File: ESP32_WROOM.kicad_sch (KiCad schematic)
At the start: 11 parts, among them J7 Programming Socket, Q1 NPN, Q2 NPN, SW1 EN, SW2 EN, U11 NTS0104GU12_115, U6 ESP32-WROOM-32E

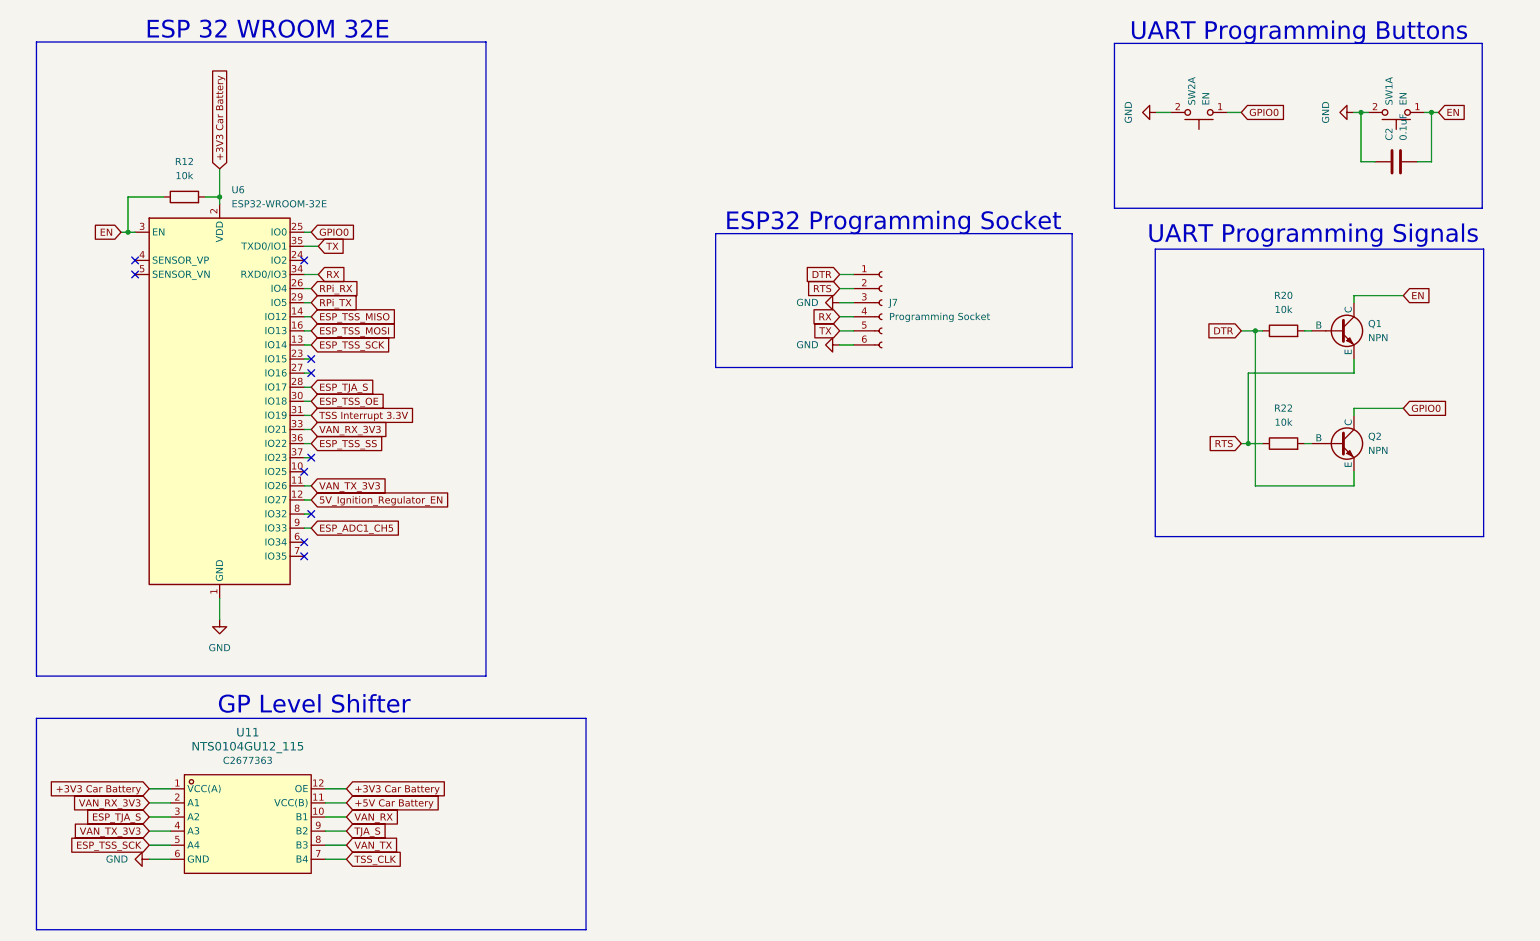
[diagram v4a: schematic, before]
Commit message: changed power regulators, updated PCB
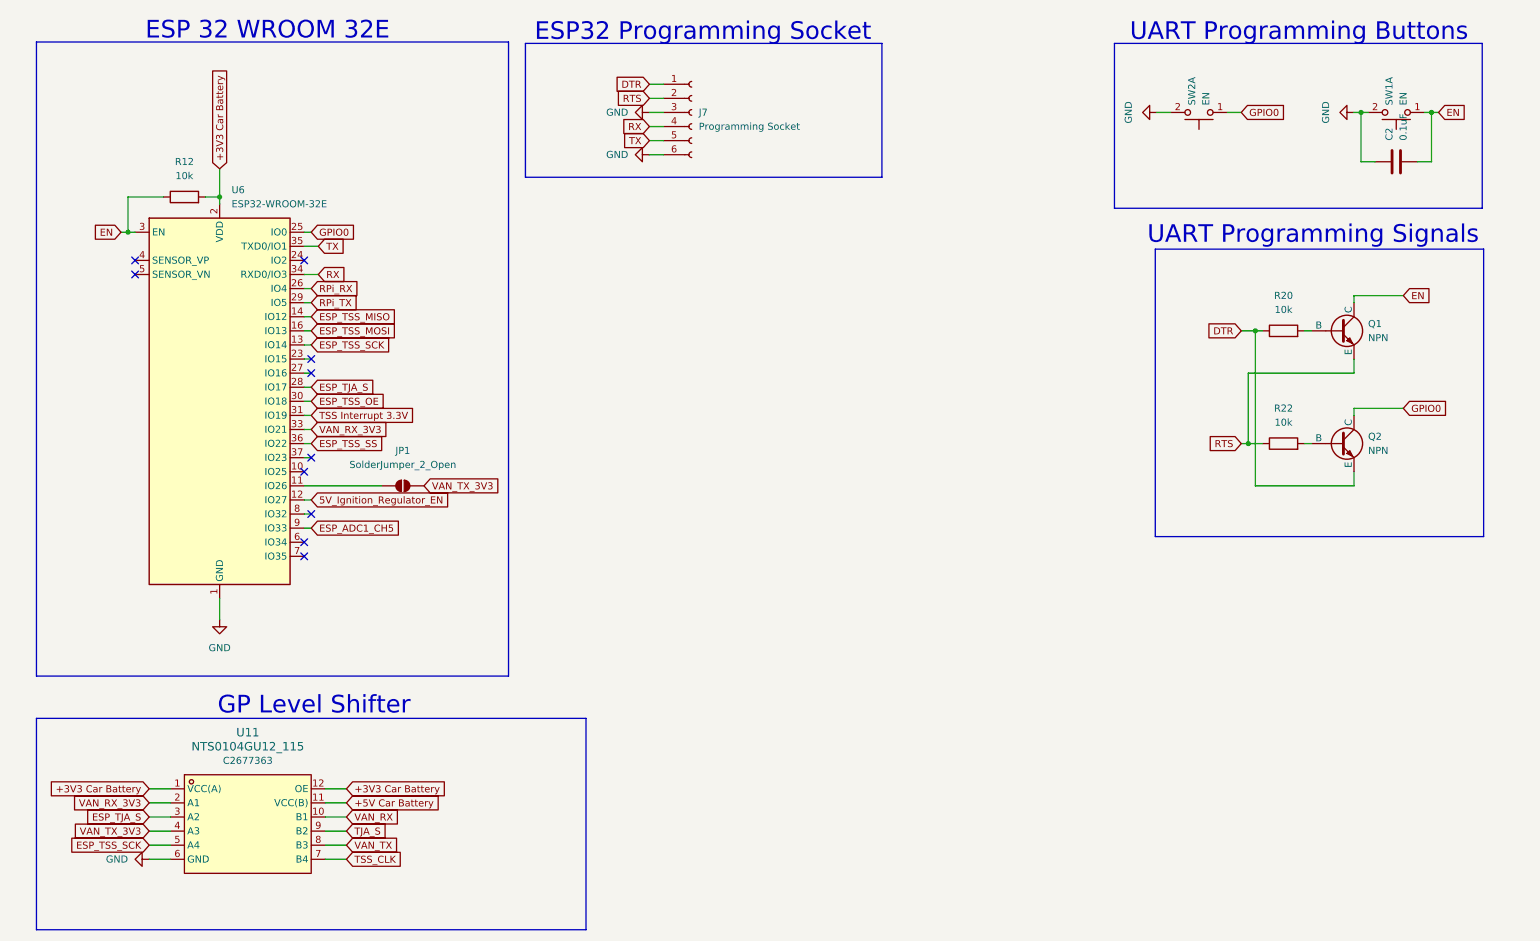
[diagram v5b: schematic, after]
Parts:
- added JP1: SolderJumper_2_Open, Jumper:SolderJumper-2_P1.3mm_Open_Pad1.0x1.5mm, symbol Jumper:SolderJumper_2_Open
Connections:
- net VAN_TX_3V3: now also JP1.2 (B); no longer U6.11 (IO26)
- new net: JP1.1 (A), U6.11 (IO26)
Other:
- moved on the sheet: J7
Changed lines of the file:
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@@
 	)
 	(rectangle
-		(start 140.208 52.324)
-		(end 204.47 76.454)
+		(start 105.918 18.034)
+		(end 170.18 42.164)
 		(stroke
 			(width 0)
@@
 	(rectangle
 		(start 17.78 17.78)
-		(end 98.806 132.08)
+		(end 102.87 132.08)
 		(stroke
 			(width 0)
@@
 	(text "ESP32 Programming Socket\n"
 		(exclude_from_sim no)
-		(at 172.212 50.292 0)
+		(at 137.922 16.002 0)
 		(effects
 			(font
@@
 	(wire
 		(pts
-			(xy 162.56 64.77) (xy 165.1 64.77)
+			(xy 128.27 30.48) (xy 130.81 30.48)
 		)
 		(stroke
@@
 	(wire
 		(pts
-			(xy 66.04 97.79) (xy 67.31 97.79)
+			(xy 66.04 97.79) (xy 80.01 97.79)
 		)
 		(stroke
@@
 	(wire
 		(pts
-			(xy 162.56 69.85) (xy 165.1 69.85)
+			(xy 128.27 35.56) (xy 130.81 35.56)
 		)
 		(stroke
@@
 	(wire
 		(pts
-			(xy 162.56 59.69) (xy 165.1 59.69)
+			(xy 128.27 25.4) (xy 130.81 25.4)
 		)
 		(stroke
@@
 	(wire
 		(pts
-			(xy 162.56 67.31) (xy 165.1 67.31)
-		)
-		(stroke
-			(width 0)
-			(type default)
-		)
-	)
-	(wire
-		(pts
-			(xy 162.56 72.39) (xy 165.1 72.39)
+			(xy 128.27 33.02) (xy 130.81 33.02)
+		)
+		(stroke
+			(width 0)
+			(type default)
+		)
+	)
+	(wire
+		(pts
+			(xy 128.27 38.1) (xy 130.81 38.1)
 		)
 		(stroke
@@
 	(wire
 		(pts
-			(xy 162.56 62.23) (xy 165.1 62.23)
+			(xy 128.27 27.94) (xy 130.81 27.94)
 		)
 		(stroke
@@
 	(global_label "TX"
 		(shape input)
-		(at 162.56 69.85 180)
+		(at 128.27 35.56 180)
 		(fields_autoplaced yes)
 		(effects
@@
 		)
 		(property "Intersheetrefs" "${INTERSHEET_REFS}"
-			(at 157.3977 69.85 0)
+			(at 123.1077 35.56 0)
 			(effects
 				(font
@@
 		)
 	)
+	(global_label "VAN_TX_3V3"
+		(shape input)
+		(at 87.63 97.79 0)
+		(fields_autoplaced yes)
+		(effects
+			(font
+				(size 1.27 1.27)
+			)
+			(justify left)
+		)
+		(property "Intersheetrefs" "${INTERSHEET_REFS}"
+			(at 101.7428 97.79 0)
+			(effects
+				(font
+					(size 1.27 1.27)
+				)
+				(justify left)
+				(hide yes)
+			)
+		)
+	)
 	(global_label "EN"
 		(shape input)
@@
 		)
 	)
-	(global_label "VAN_TX_3V3"
-		(shape input)
-		(at 67.31 97.79 0)
-		(fields_autoplaced yes)
-		(effects
-			(font
-				(size 1.27 1.27)
-			)
-			(justify left)
-		)
-		(property "Intersheetrefs" "${INTERSHEET_REFS}"
-			(at 81.4228 97.79 0)
-			(effects
-				(font
-					(size 1.27 1.27)
-				)
-				(justify left)
-				(hide yes)
-			)
-		)
-	)
 	(global_label "EN"
 		(shape input)
@@
 	(global_label "RX"
 		(shape input)
-		(at 162.56 67.31 180)
+		(at 128.27 33.02 180)
 		(fields_autoplaced yes)
 		(effects
@@
 		)
 		(property "Intersheetrefs" "${INTERSHEET_REFS}"
-			(at 157.0953 67.31 0)
+			(at 122.8053 33.02 0)
 			(effects
 				(font
@@
 	(global_label "RTS"
 		(shape input)
-		(at 162.56 62.23 180)
+		(at 128.27 27.94 180)
 		(fields_autoplaced yes)
 		(effects
@@
 		)
 		(property "Intersheetrefs" "${INTERSHEET_REFS}"
-			(at 156.1277 62.23 0)
+			(at 121.8377 27.94 0)
 			(effects
 				(font
@@
 	(global_label "DTR"
 		(shape input)
-		(at 162.56 59.69 180)
+		(at 128.27 25.4 180)
 		(fields_autoplaced yes)
 		(effects
@@
 		)
 		(property "Intersheetrefs" "${INTERSHEET_REFS}"
-			(at 156.0672 59.69 0)
+			(at 121.7772 25.4 0)
 			(effects
 				(font
@@
 	(symbol
 		(lib_id "power:GND")
-		(at 162.56 72.39 270)
+		(at 128.27 38.1 270)
 		(unit 1)
 		(exclude_from_sim no)
@@
 		(fields_autoplaced yes)
 		(property "Reference" "#PWR090"
-			(at 156.21 72.39 0)
+			(at 121.92 38.1 0)
 			(effects
 				(font
@@
 		)
 		(property "Value" "GND"
-			(at 158.75 72.3899 90)
+			(at 124.46 38.0999 90)
 			(effects
 				(font
@@
 		)
 		(property "Footprint" ""
-			(at 162.56 72.39 0)
+			(at 128.27 38.1 0)
 			(effects
 				(font
@@
 		)
 		(property "Datasheet" ""
-			(at 162.56 72.39 0)
+			(at 128.27 38.1 0)
 			(effects
 				(font
@@
 		)
 		(property "Description" "Power symbol creates a global label with name \"GND\" , ground"
-			(at 162.56 72.39 0)
+			(at 128.27 38.1 0)
 			(effects
 				(font
@@
 	)
 	(symbol
+		(lib_id "Jumper:SolderJumper_2_Open")
+		(at 83.82 97.79 0)
+		(unit 1)
+		(exclude_from_sim no)
+		(in_bom no)
+		(on_board yes)
+		(dnp no)
+		(fields_autoplaced yes)
+		(property "Reference" "JP1"
+			(at 83.82 91.44 0)
+			(effects
+				(font
+					(size 1.27 1.27)
+				)
+			)
+		)
+		(property "Value" "SolderJumper_2_Open"
+			(at 83.82 93.98 0)
+			(effects
+				(font
+					(size 1.27 1.27)
+				)
+			)
+		)
+		(property "Footprint" "Jumper:SolderJumper-2_P1.3mm_Open_Pad1.0x1.5mm"
+			(at 83.82 97.79 0)
+			(effects
+				(font
+					(size 1.27 1.27)
+				)
+				(hide yes)
+			)
+		)
+		(property "Datasheet" "~"
+			(at 83.82 97.79 0)
+			(effects
+				(font
+					(size 1.27 1.27)
+				)
+				(hide yes)
+			)
+		)
+		(property "Description" "Solder Jumper, 2-pole, open"
+			(at 83.82 97.79 0)
+			(effects
+				(font
+					(size 1.27 1.27)
+				)
+				(hide yes)
+			)
+		)
+		(pin "2"
+		)
+		(pin "1"
+		)
+		(instances
+			(project ""
+				(path "/3ec17d1d-183f-42c7-9d9d-808fb8c0b5df/821b1801-1173-4ad6-9af8-a86cd2d3359b"
+					(reference "JP1")
+					(unit 1)
+				)
+			)
+		)
+	)
+	(symbol
 		(lib_id "power:GND")
-		(at 162.56 64.77 270)
+		(at 128.27 30.48 270)
 		(unit 1)
 		(exclude_from_sim no)
@@
 		(fields_autoplaced yes)
 		(property "Reference" "#PWR089"
-			(at 156.21 64.77 0)
+			(at 121.92 30.48 0)
 			(effects
 				(font
@@
 		)
 		(property "Value" "GND"
-			(at 158.75 64.7699 90)
+			(at 124.46 30.4799 90)
 			(effects
 				(font
@@
 		)
 		(property "Footprint" ""
-			(at 162.56 64.77 0)
+			(at 128.27 30.48 0)
 			(effects
 				(font
@@
 		)
 		(property "Datasheet" ""
-			(at 162.56 64.77 0)
+			(at 128.27 30.48 0)
 			(effects
 				(font
@@
 		)
 		(property "Description" "Power symbol creates a global label with name \"GND\" , ground"
-			(at 162.56 64.77 0)
+			(at 128.27 30.48 0)
 			(effects
 				(font
@@
 	(symbol
 		(lib_id "Connector:Conn_01x06_Socket")
-		(at 170.18 64.77 0)
+		(at 135.89 30.48 0)
 		(unit 1)
 		(exclude_from_sim no)
@@
 		(fields_autoplaced yes)
 		(property "Reference" "J7"
-			(at 171.45 64.7699 0)
+			(at 137.16 30.4799 0)
 			(effects
 				(font
@@
 		)
 		(property "Value" "Programming Socket"
-			(at 171.45 67.3099 0)
+			(at 137.16 33.0199 0)
 			(effects
 				(font
@@
 		)
 		(property "Footprint" "Connector_JST:JST_GH_SM06B-GHS-TB_1x06-1MP_P1.25mm_Horizontal"
-			(at 170.18 64.77 0)
+			(at 135.89 30.48 0)
 			(effects
 				(font
@@
 		)
 		(property "Datasheet" "~"
-			(at 170.18 64.77 0)
+			(at 135.89 30.48 0)
 			(effects
 				(font
@@
 		)
 		(property "Description" "Generic connector, single row, 01x06, script generated"
-			(at 170.18 64.77 0)
-			(effects
-				(font
+			(at 135.89 30.48 0)
+			(effects
+				(font

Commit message: switched to vertial program connector, changed logo position
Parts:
- J7: footprint Connector_JST:JST_GH_SM06B-GHS-TB_1x06-1MP_P1.25mm_Horizontal -> Connector_JST:JST_GH_BM06B-GHS-TBT_1x06-1MP_P1.25mm_Vertical
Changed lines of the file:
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@@
 			)
 		)
-		(property "Footprint" "Connector_JST:JST_GH_SM06B-GHS-TB_1x06-1MP_P1.25mm_Horizontal"
+		(property "Footprint" "Connector_JST:JST_GH_BM06B-GHS-TBT_1x06-1MP_P1.25mm_Vertical"
 			(at 135.89 30.48 0)
 			(effects

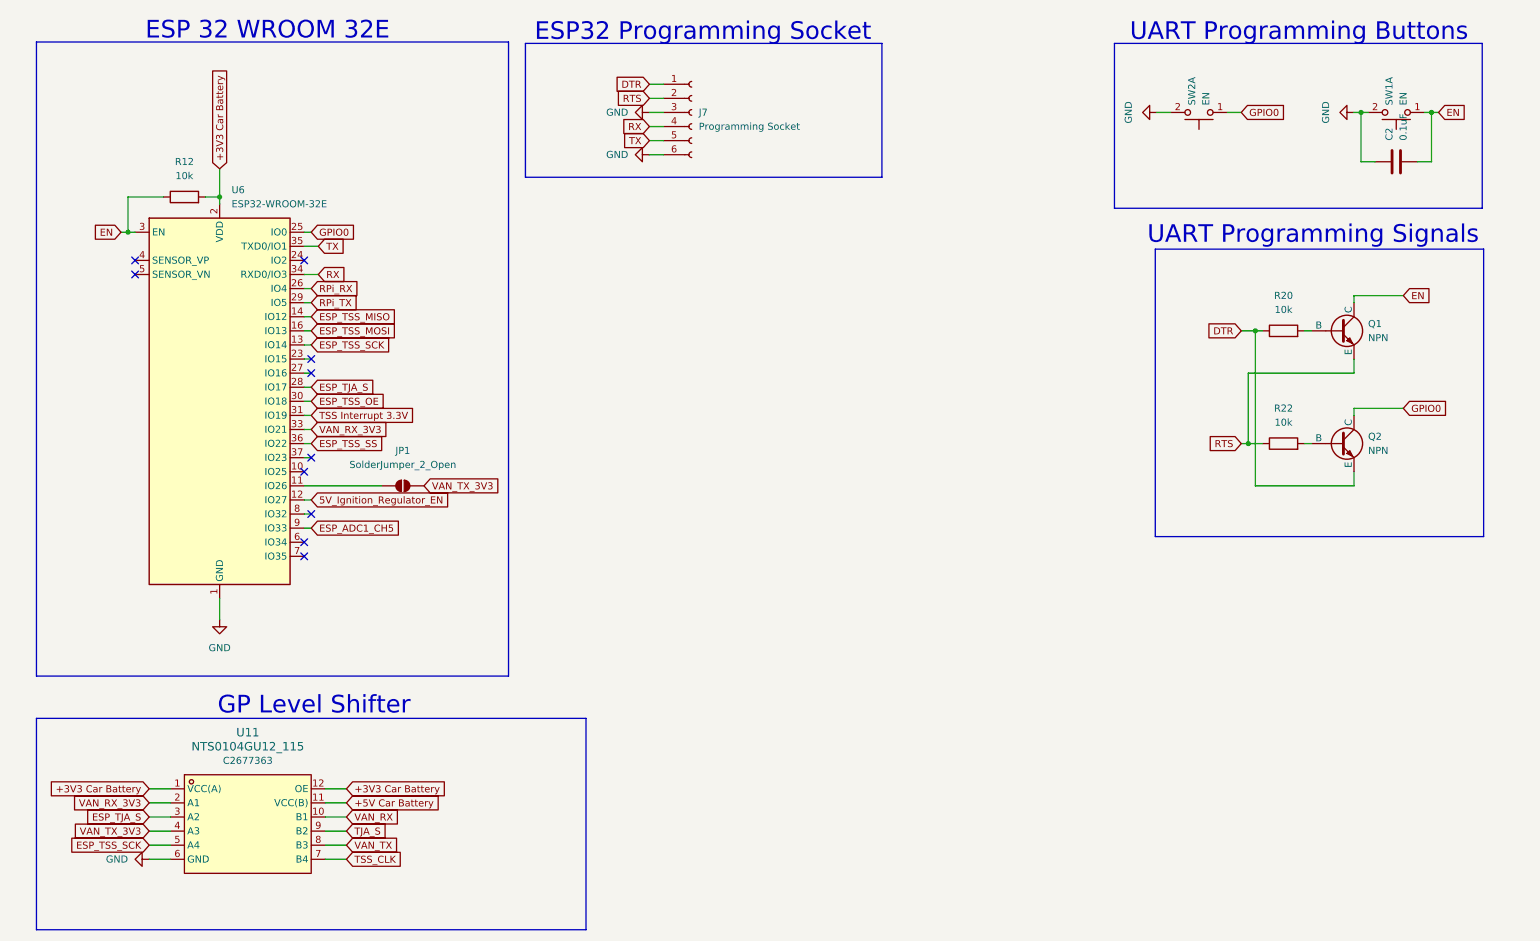
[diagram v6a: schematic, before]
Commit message: added tvs diodes, 100nF, pull-up for TSS interrupt
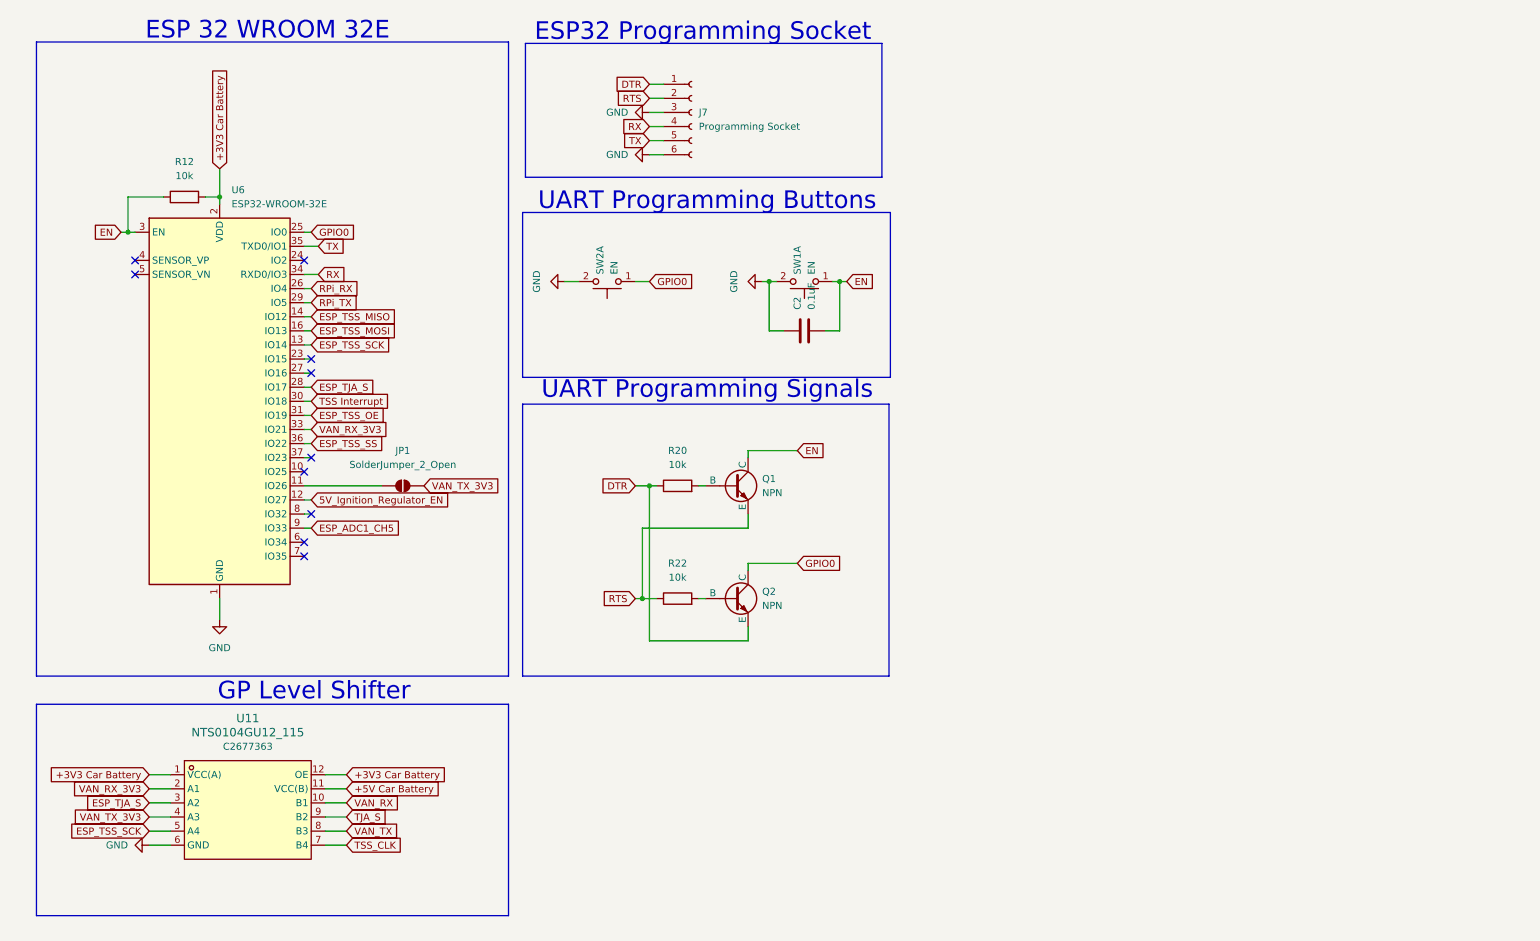
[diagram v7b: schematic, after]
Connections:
- net TSS Interrupt 3.3V is gone; now on net ESP_TSS_OE: U6.31 (IO19)
- net ESP_TSS_OE: no longer U6.30 (IO18)
- new net TSS Interrupt: U6.30 (IO18)
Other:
- moved on the sheet: C2, Q1, Q2, R20, R22, SW1A, SW2A, U11

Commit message: Change inductor type.
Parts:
- U6: footprint intoftainment:esp32_altered -> RF_Module:ESP32-WROOM-32D
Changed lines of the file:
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@@
 			)
 		)
-		(property "Footprint" "intoftainment:esp32_altered"
+		(property "Footprint" "RF_Module:ESP32-WROOM-32D"
 			(at 67.31 116.84 0)
 			(effects
